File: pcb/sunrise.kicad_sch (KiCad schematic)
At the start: 9 parts, among them J1 Conn_01x15_Female, J2 Conn_01x15_Female, J3 Conn_01x04_Female, Q1 TSM2302CX, Q2 TSM2302CX, Q3 TSM2302CX

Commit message: Updated schematic and footprints
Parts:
- added R2, R3: R, Resistor_SMD:R_0805_2012Metric, symbol Device:R
- J1: footprint Connector_PinHeader_1.27mm:PinHeader_1x15_P1.27mm_Vertical -> Connector_PinSocket_2.54mm:PinSocket_1x15_P2.54mm_Vertical
- J2: footprint (none) -> Connector_PinSocket_2.54mm:PinSocket_1x15_P2.54mm_Vertical
- gave numbers to parts that had none: 2
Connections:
- net +5V: now also J2.15 (Pin_15)
- net GND: now also J2.14 (Pin_14)
- net Red_IO: no longer R1.1
- net GREEN_IO: now reaches J2.11 (Pin_11)
- net GREEN_IO: now also R2.1
- net BLUE_IO: now reaches J2.12 (Pin_12)
- net BLUE_IO: now also R3.1
- net RED_IO: now reaches J2.13 (Pin_13)
- net RED_IO: now also R1.1
- net Blue_IO: no longer names the net of Q3.1 (G)
- net Blue_IO: now also R3.2
- net Green_IO: no longer names the net of Q2.1 (G)
- net Green_IO: now also R2.2
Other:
- moved on the sheet: J1, J2, J3, J4, Q1, Q2, Q3, R1, U1

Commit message: Added resistor
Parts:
- added R5k6: R, Resistor_SMD:R_0805_2012Metric, symbol Device:R
- added R? (x2): 5k6, Resistor_SMD:R_0805_2012Metric, symbol Device:R
- R1, R2, R3: value R -> 560
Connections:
- net BLUE_IO: now also R?.1
- net GND: now also R5k6.2, R?.2, R?.2
- net GREEN_IO: now also R?.1
- net RED_IO: now also R5k6.1

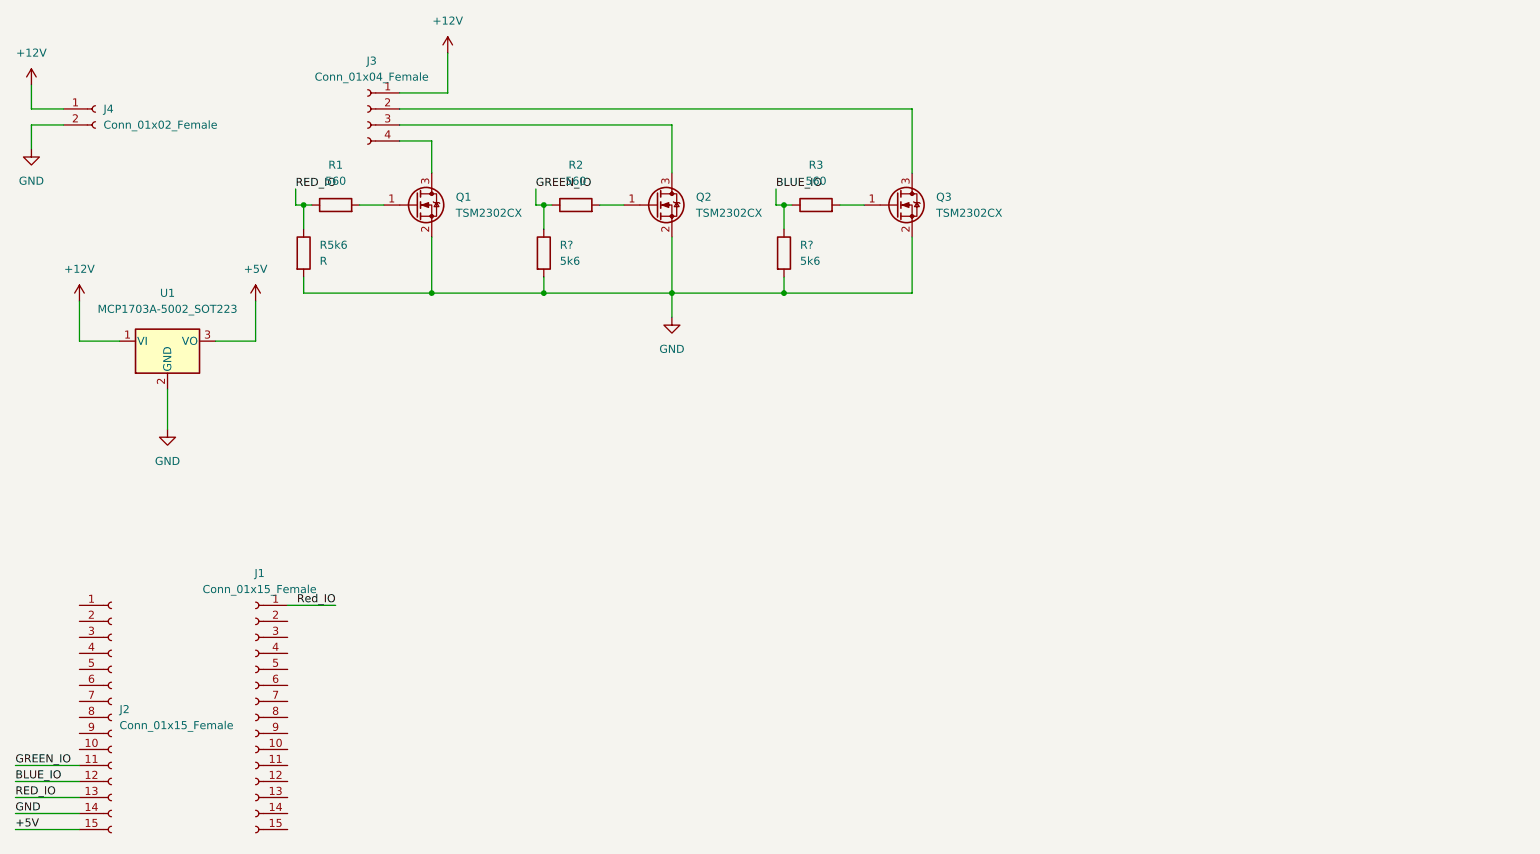
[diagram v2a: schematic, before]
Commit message: Corrected schematic and finished layout
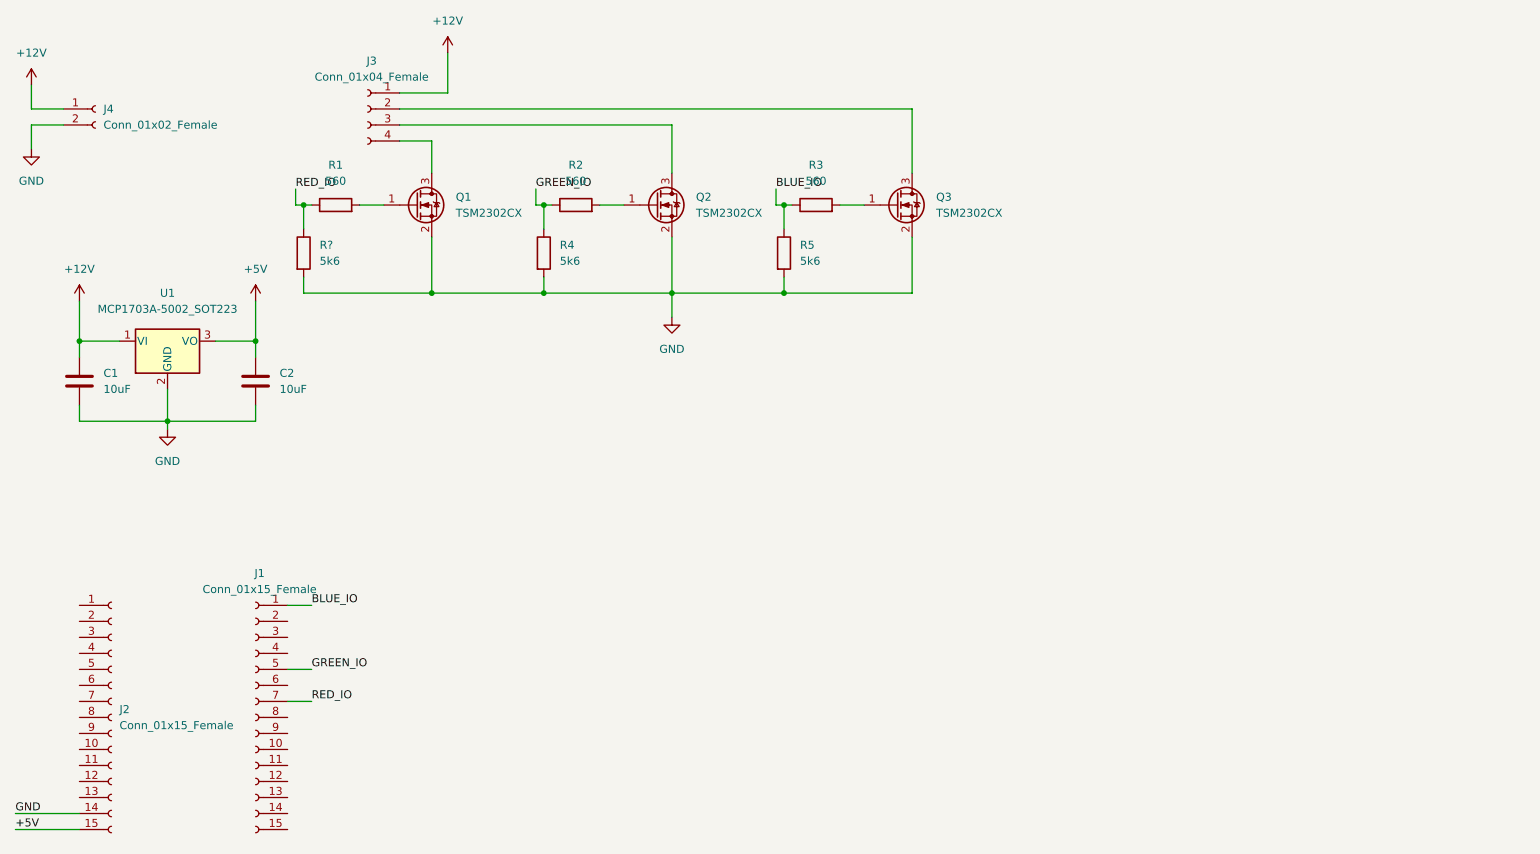
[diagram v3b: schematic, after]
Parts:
- added C1, C2: 10uF, Capacitor_SMD:C_0805_2012Metric, symbol Device:C
- J3: footprint Connector_PinHeader_1.27mm:PinHeader_1x03_P1.27mm_Vertical -> Connector_PinHeader_1.27mm:PinHeader_1x04_P1.27mm_Vertical
- J4: footprint (none) -> Connector_PinHeader_1.27mm:PinHeader_1x02_P1.27mm_Vertical
- R?: renamed from R5k6; value R -> 5k6
- gave numbers to parts that had none: 2
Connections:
- net Red_IO is gone; now on net BLUE_IO: J1.1 (Pin_1)
- net +12V: now also C1.1
- net +5V: now also C2.1
- net BLUE_IO: no longer J2.12 (Pin_12)
- net GND: now also C1.2, C2.2
- net GREEN_IO: now also J1.5 (Pin_5); no longer J2.11 (Pin_11)
- net RED_IO: now also J1.7 (Pin_7); no longer J2.13 (Pin_13)

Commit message: Final
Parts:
- gave numbers to parts that had none: 1
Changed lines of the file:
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@@
   (symbol (lib_id "Device:R") (at 66.04 53.34 0) (unit 1)
     (in_bom yes) (on_board yes) (fields_autoplaced)
-    (property "Reference" "R?" (id 0) (at 68.58 52.0699 0)
+    (property "Reference" "R6" (id 0) (at 68.58 52.0699 0)
       (effects (font (size 1.27 1.27)) (justify left))
     )
@@
     )
     (path "/94a7379f-0759-4af3-b86c-c3a01b2bb6ad"
-      (reference "R?") (unit 1) (value "5k6") (footprint "Resistor_SMD:R_0805_2012Metric")
+      (reference "R6") (unit 1) (value "5k6") (footprint "Resistor_SMD:R_0805_2012Metric")
     )
     (path "/100708ee-4125-4f5a-b2e4-ac3378e710a6"

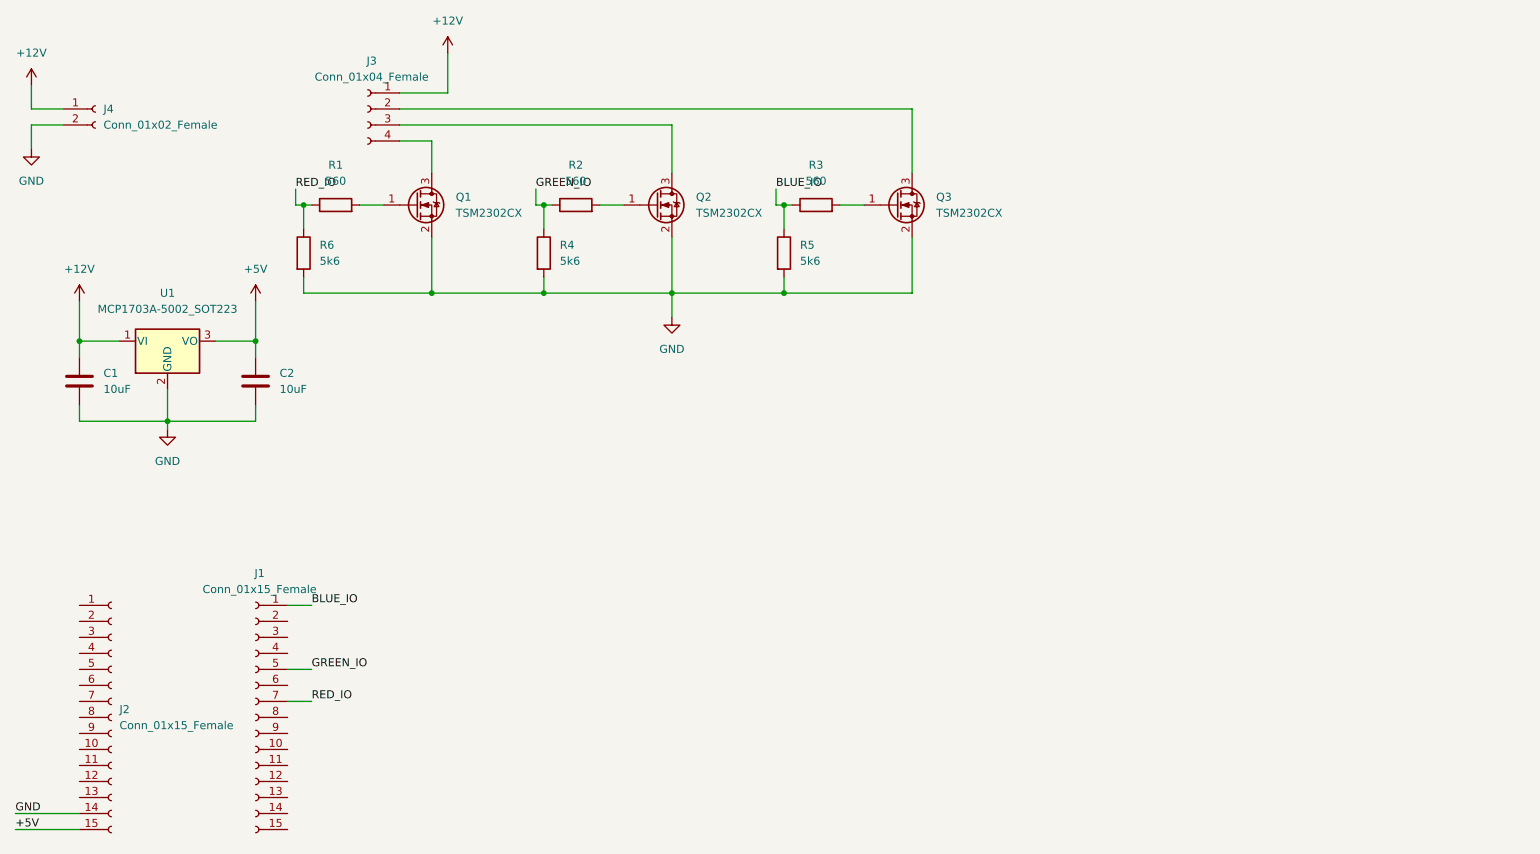
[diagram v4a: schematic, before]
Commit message: Added IR receiver
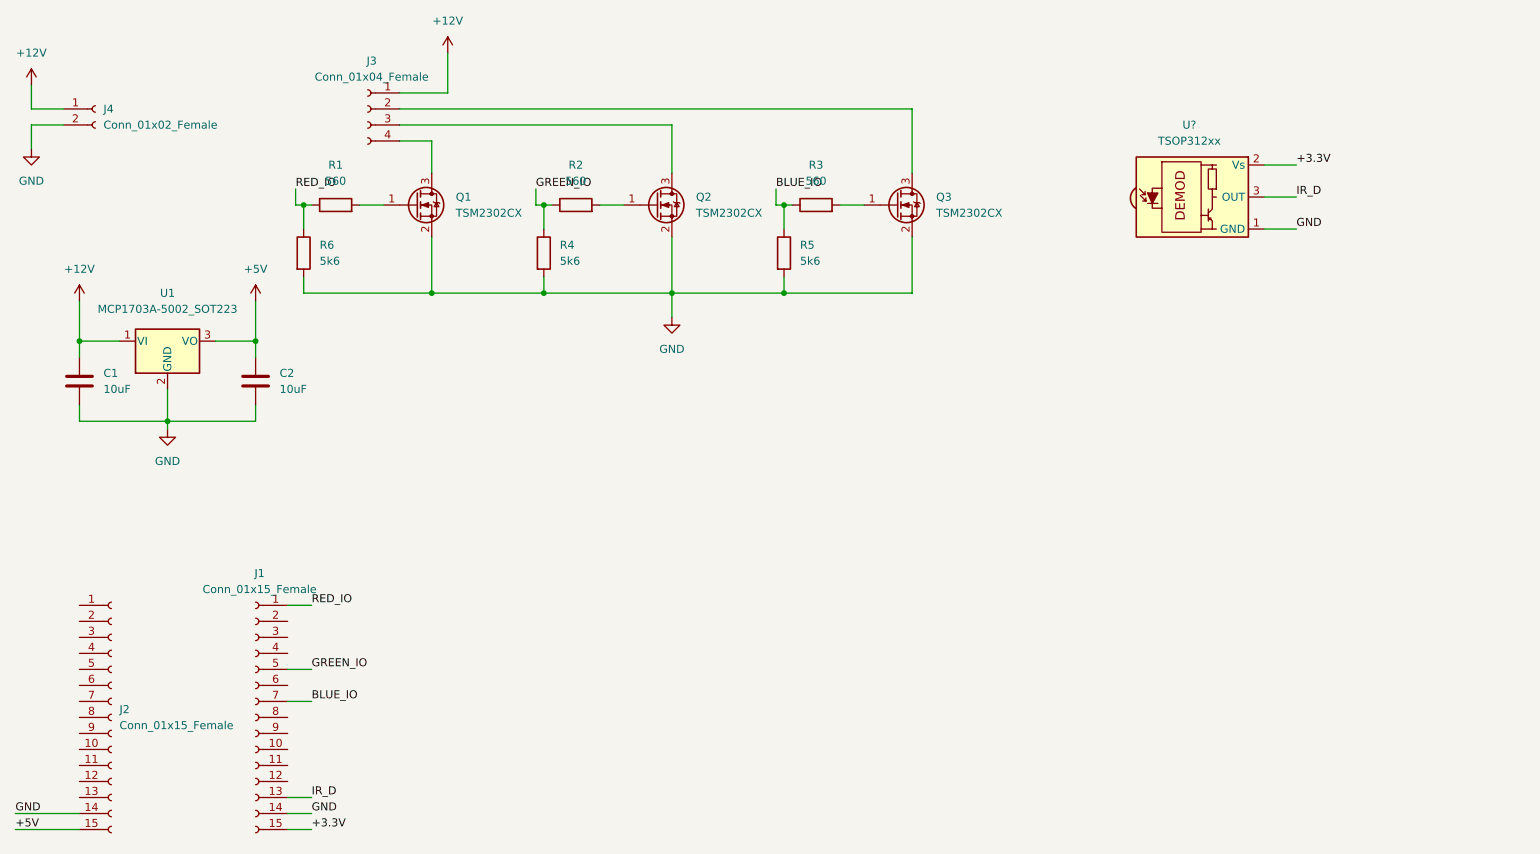
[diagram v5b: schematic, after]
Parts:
- added U?: TSOP312xx, OptoDevice:Vishay_CAST-3Pin, symbol Interface_Optical:TSOP312xx
- J3: footprint Connector_PinHeader_1.27mm:PinHeader_1x04_P1.27mm_Vertical -> Connector_PinHeader_2.54mm:PinHeader_1x04_P2.54mm_Vertical
- J4: footprint Connector_PinHeader_1.27mm:PinHeader_1x02_P1.27mm_Vertical -> Connector_PinHeader_2.54mm:PinHeader_1x02_P2.54mm_Vertical
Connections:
- net BLUE_IO: now also J1.7 (Pin_7); no longer J1.1 (Pin_1)
- net GND: now also J1.14 (Pin_14), U?.1 (GND)
- net RED_IO: now also J1.1 (Pin_1); no longer J1.7 (Pin_7)
- net IR_D: now reaches J1.13 (Pin_13)
- net IR_D: now also U?.3 (OUT)
- net +3.3V: now reaches J1.15 (Pin_15)
- net +3.3V: now also U?.2 (Vs)
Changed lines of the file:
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@@
+    (stroke (width 0) (type default) (color 0 0 0 0))
+  )
+  (wire (pts (xy 63.5 139.7) (xy 67.31 139.7))
     (stroke (width 0) (type default) (color 0 0 0 0))
   )
@@
     (stroke (width 0) (type default) (color 0 0 0 0))
   )
+  (wire (pts (xy 218.44 49.53) (xy 223.52 49.53))
+    (stroke (width 0) (type default) (color 0 0 0 0))
+  )
   (wire (pts (xy 22.86 26.67) (xy 22.86 30.48))
     (stroke (width 0) (type default) (color 0 0 0 0))
@@
     (stroke (width 0) (type default) (color 0 0 0 0))
   )
+  (wire (pts (xy 63.5 144.78) (xy 67.31 144.78))
+    (stroke (width 0) (type default) (color 0 0 0 0))
+  )
+  (wire (pts (xy 218.44 44.45) (xy 223.52 44.45))
+    (stroke (width 0) (type default) (color 0 0 0 0))
+  )
+  (wire (pts (xy 63.5 124.46) (xy 67.31 124.46))
+    (stroke (width 0) (type default) (color 0 0 0 0))
+  )
+  (wire (pts (xy 151.13 45.72) (xy 154.94 45.72))
+    (stroke (width 0) (type default) (color 0 0 0 0))
+  )
+  (wire (pts (xy 30.48 67.31) (xy 30.48 60.96))
+    (stroke (width 0) (type default) (color 0 0 0 0))
+  )
+  (wire (pts (xy 102.87 43.18) (xy 102.87 45.72))
+    (stroke (width 0) (type default) (color 0 0 0 0))
+  )
+  (wire (pts (xy 58.42 80.01) (xy 44.45 80.01))
+    (stroke (width 0) (type default) (color 0 0 0 0))
+  )
+  (wire (pts (xy 218.44 39.37) (xy 223.52 39.37))
+    (stroke (width 0) (type default) (color 0 0 0 0))
+  )
+  (wire (pts (xy 74.93 45.72) (xy 78.74 45.72))
+    (stroke (width 0) (type default) (color 0 0 0 0))
+  )
+  (wire (pts (xy 140.97 43.18) (xy 140.97 45.72))
+    (stroke (width 0) (type default) (color 0 0 0 0))
+  )
   (wire (pts (xy 63.5 109.22) (xy 67.31 109.22))
     (stroke (width 0) (type default) (color 0 0 0 0))
   )
-  (wire (pts (xy 151.13 45.72) (xy 154.94 45.72))
-    (stroke (width 0) (type default) (color 0 0 0 0))
-  )
-  (wire (pts (xy 30.48 67.31) (xy 30.48 60.96))
-    (stroke (width 0) (type default) (color 0 0 0 0))
-  )
-  (wire (pts (xy 102.87 43.18) (xy 102.87 45.72))
-    (stroke (width 0) (type default) (color 0 0 0 0))
-  )
-  (wire (pts (xy 58.42 80.01) (xy 44.45 80.01))
-    (stroke (width 0) (type default) (color 0 0 0 0))
-  )
-  (wire (pts (xy 74.93 45.72) (xy 78.74 45.72))
-    (stroke (width 0) (type default) (color 0 0 0 0))
-  )
-  (wire (pts (xy 140.97 43.18) (xy 140.97 45.72))
-    (stroke (width 0) (type default) (color 0 0 0 0))
-  )
-  (wire (pts (xy 63.5 124.46) (xy 67.31 124.46))
-    (stroke (width 0) (type default) (color 0 0 0 0))
-  )
   (wire (pts (xy 58.42 67.31) (xy 58.42 60.96))
     (stroke (width 0) (type default) (color 0 0 0 0))
@@
     (stroke (width 0) (type default) (color 0 0 0 0))
   )
+  (wire (pts (xy 63.5 142.24) (xy 67.31 142.24))
+    (stroke (width 0) (type default) (color 0 0 0 0))
+  )
   (wire (pts (xy 104.14 45.72) (xy 105.41 45.72))
     (stroke (width 0) (type default) (color 0 0 0 0))
   )
+  (label "+3.3V" (at 67.31 144.78 0)
+    (effects (font (size 1.27 1.27)) (justify left bottom))
+  )
+  (label "GND" (at 223.52 49.53 0)
+    (effects (font (size 1.27 1.27)) (justify left bottom))
+  )
+  (label "IR_D" (at 67.31 139.7 0)
+    (effects (font (size 1.27 1.27)) (justify left bottom))
+  )
   (label "GND" (at 20.32 142.24 0)
     (effects (font (size 1.27 1.27)) (justify left bottom))
@@
     (effects (font (size 1.27 1.27)) (justify left bottom))
   )
+  (label "+3.3V" (at 223.52 39.37 0)
+    (effects (font (size 1.27 1.27)) (justify left bottom))
+  )
   (label "RED_IO" (at 64.77 43.18 0)
     (effects (font (size 1.27 1.27)) (justify left bottom))
   )
-  (label "BLUE_IO" (at 67.31 109.22 0)
-    (effects (font (size 1.27 1.27)) (justify left bottom))
-  )
-  (label "RED_IO" (at 67.31 124.46 0)
+  (label "BLUE_IO" (at 67.31 124.46 0)
+    (effects (font (size 1.27 1.27)) (justify left bottom))
+  )
+  (label "RED_IO" (at 67.31 109.22 0)
+    (effects (font (size 1.27 1.27)) (justify left bottom))
+  )
+  (label "GND" (at 67.31 142.24 0)
     (effects (font (size 1.27 1.27)) (justify left bottom))
   )
@@
   )
   (label "BLUE_IO" (at 140.97 43.18 0)
+    (effects (font (size 1.27 1.27)) (justify left bottom))
+  )
+  (label "IR_D" (at 223.52 44.45 0)
     (effects (font (size 1.27 1.27)) (justify left bottom))
   )
@@
     (property "Reference" "J3" (id 0) (at 76.835 22.86 0))
     (property "Value" "Conn_01x04_Female" (id 1) (at 76.835 25.4 0))
-    (property "Footprint" "Connector_PinHeader_1.27mm:PinHeader_1x04_P1.27mm_Vertical" (id 2) (at 76.2 30.48 0)
+    (property "Footprint" "Connector_PinHeader_2.54mm:PinHeader_1x04_P2.54mm_Vertical" (id 2) (at 76.2 30.48 0)
       (effects (font (size 1.27 1.27)) hide)
     )
@@
     (pin "2")
   )
+  (symbol (lib_id "Interface_Optical:TSOP312xx") (at 208.28 44.45 0) (unit 1)
+    (in_bom yes) (on_board yes) (fields_autoplaced)
+    (property "Reference" "U?" (id 0) (at 206.545 33.02 0))
+    (property "Value" "TSOP312xx" (id 1) (at 206.545 35.56 0))
+    (property "Footprint" "OptoDevice:Vishay_CAST-3Pin" (id 2) (at 207.01 53.975 0)
+      (effects (font (size 1.27 1.27)) hide)
+    )
+    (property "Datasheet" "http://www.vishay.com/docs/82492/tsop312.pdf" (id 3) (at 224.79 36.83 0)
+      (effects (font (size 1.27 1.27)) hide)
+    )
+    (pin "1")
+    (pin "2")
+    (pin "3")
+  )
   (symbol (lib_id "Transistor_FET:TSM2302CX") (at 160.02 45.72 0) (unit 1)
     (in_bom yes) (on_board yes) (fields_autoplaced)
@@
       (effects (font (size 1.27 1.27)) (justify left))
     )
-    (property "Footprint" "Connector_PinHeader_1.27mm:PinHeader_1x02_P1.27mm_Vertical" (id 2) (at 33.02 30.48 0)
+    (property "Footprint" "Connector_PinHeader_2.54mm:PinHeader_1x02_P2.54mm_Vertical" (id 2) (at 33.02 30.48 0)
       (effects (font (size 1.27 1.27)) hide)
     )
@@
     )
     (path "/5c1ffb20-b0a8-454d-9261-c38dd40450f8"
-      (reference "J3") (unit 1) (value "Conn_01x04_Female") (footprint "Connector_PinHeader_1.27mm:PinHeader_1x04_P1.27mm_Vertical")
+      (reference "J3") (unit 1) (value "Conn_01x04_Female") (footprint "Connector_PinHeader_2.54mm:PinHeader_1x04_P2.54mm_Vertical")
     )
     (path "/f5507b8e-4f1b-4dd8-8659-eb414f58152e"
-      (reference "J4") (unit 1) (value "Conn_01x02_Female") (footprint "Connector_PinHeader_1.27mm:PinHeader_1x02_P1.27mm_Vertical")
+      (reference "J4") (unit 1) (value "Conn_01x02_Female") (footprint "Connector_PinHeader_2.54mm:PinHeader_1x02_P2.54mm_Vertical")
     )
     (path "/760be3e8-10d1-445c-a20b-02fba00981fa"
@@
       (reference "U1") (unit 1) (value "MCP1703A-5002_SOT223") (footprint "Package_TO_SOT_SMD:SOT-223-3_TabPin2")
     )
-  )
+    (path "/a92c3364-2905-48b6-9985-28ad44e8c845"
+      (reference "U?") (unit 1) (value "TSOP312xx") (footprint "OptoDevice:Vishay_CAST-3Pin")
+    )
+  )

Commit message: Updated pcb
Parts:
- gave numbers to parts that had none: 1
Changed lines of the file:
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@@
   (symbol (lib_id "Interface_Optical:TSOP312xx") (at 208.28 44.45 0) (unit 1)
     (in_bom yes) (on_board yes) (fields_autoplaced)
-    (property "Reference" "U?" (id 0) (at 206.545 33.02 0))
+    (property "Reference" "U2" (id 0) (at 206.545 33.02 0))
     (property "Value" "TSOP312xx" (id 1) (at 206.545 35.56 0))
     (property "Footprint" "OptoDevice:Vishay_CAST-3Pin" (id 2) (at 207.01 53.975 0)
@@
     )
     (path "/a92c3364-2905-48b6-9985-28ad44e8c845"
-      (reference "U?") (unit 1) (value "TSOP312xx") (footprint "OptoDevice:Vishay_CAST-3Pin")
-    )
-  )
+      (reference "U2") (unit 1) (value "TSOP312xx") (footprint "OptoDevice:Vishay_CAST-3Pin")
+    )
+  )
